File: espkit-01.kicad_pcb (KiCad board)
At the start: 2 copper layers, 20 x 35.7 mm, 24 parts, among them IC1 WS2812B, P1 ESP-01, P2 BREAKOUT, P3 USB_5PIN_SHELL, P4 PWR, P5 NEOPIXEL, P6 BRIDGE, Q1 S8050, Q2 S8050, SW1 RESET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

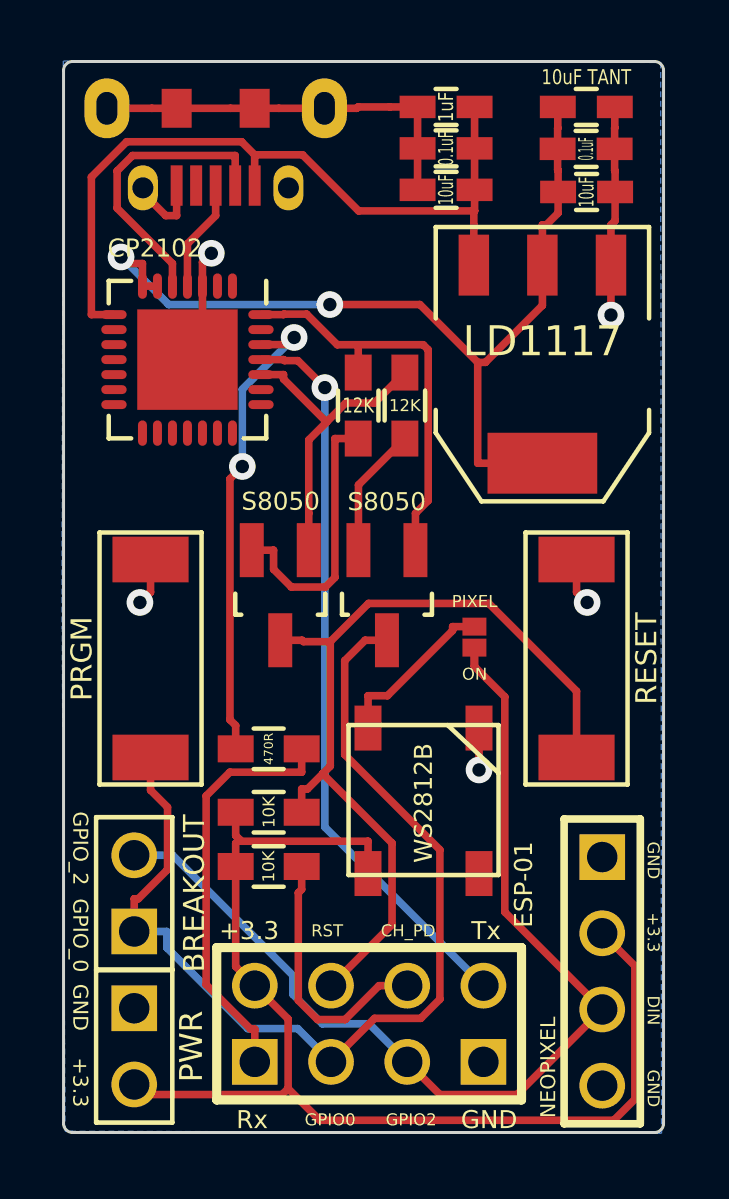
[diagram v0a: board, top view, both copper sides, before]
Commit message: Sometimes helps to connect your grounds.
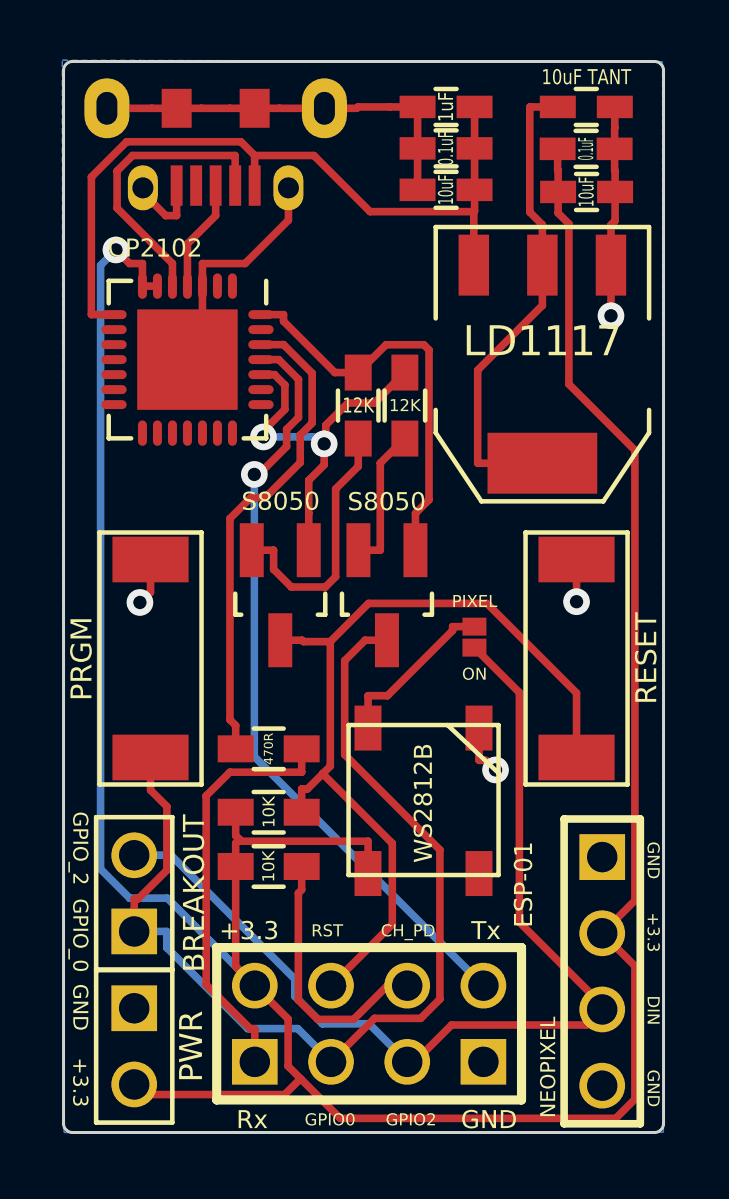
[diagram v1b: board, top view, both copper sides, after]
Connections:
- C1 pad 1: +3V3 -> +3.3V
- C4 pad 1: +3V3 -> +3.3V
- U2 pad 6: +3V3 -> +3.3V
- U2 pad 7: +3V3 -> +3.3V
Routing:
- net +3.3V: track 39.0 -> 96.7 mm, vias 0 -> 1
- net +3V3: track 30.8 -> 16.0 mm, vias 2 -> 0
- net GND: track 35.4 -> 39.7 mm, vias 5 -> 4
- net /RTS: track 10.7 -> 12.9 mm, vias 0 -> 2
- net /GPIO2: track 34.9 -> 33.3 mm
- net /RXD: track 24.6 -> 25.6 mm
- net Net-(R5-Pad2): track 15.9 -> 16.1 mm, vias 2 -> 0
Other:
- net class 2.0mm removed
